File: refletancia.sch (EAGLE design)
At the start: 27 parts

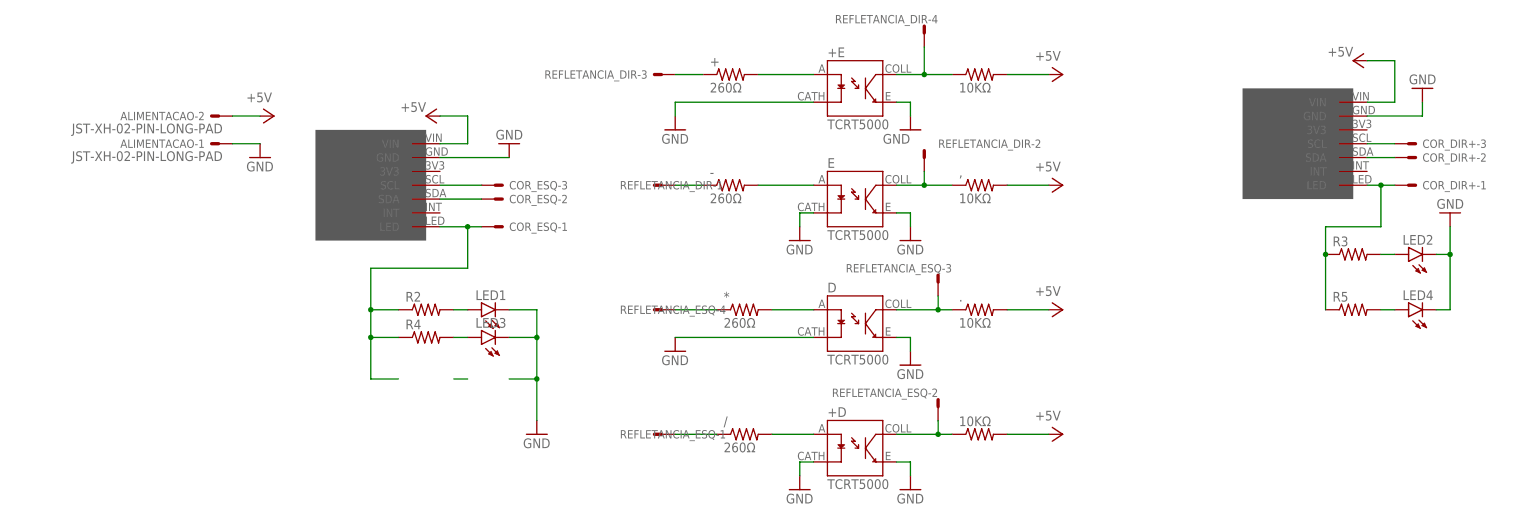
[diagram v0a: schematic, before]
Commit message: Alteração da dimensão e posição de furos
Os furos de fixação foram alterados, a posição dos conectores do sensor de cor também foi alterada, a dimensão da placa também foi alterada assim como posição de várias trilhas foi trocada
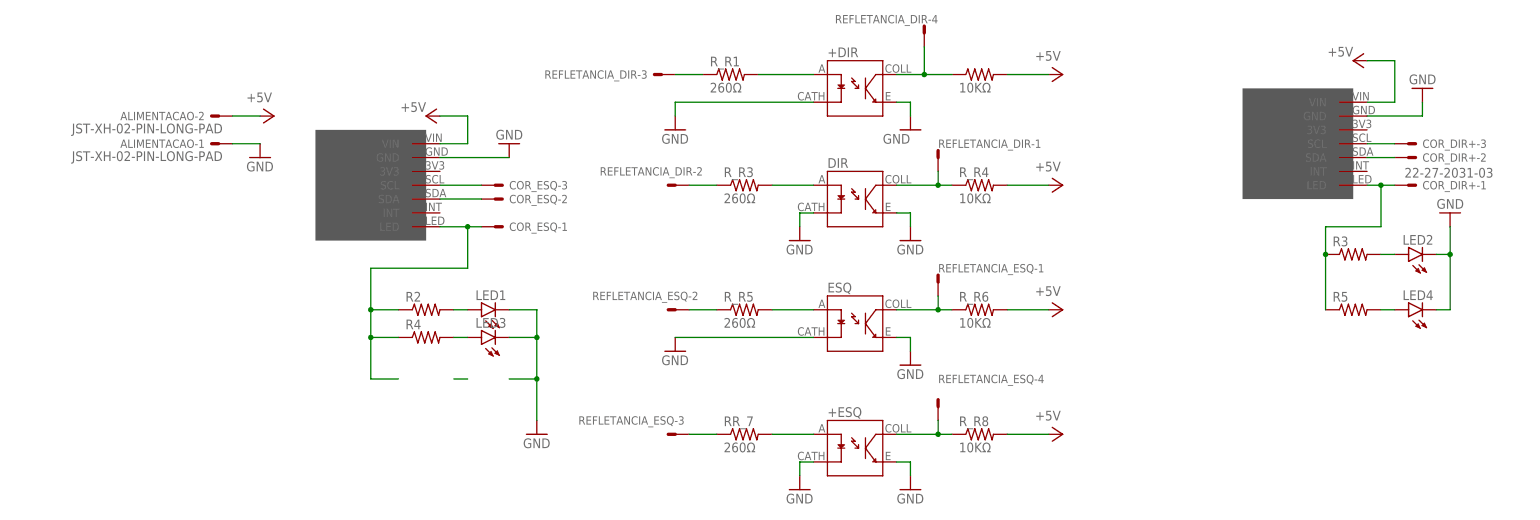
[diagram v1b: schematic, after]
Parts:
- removed -: 260Ω, rcl_robotica:R-US_0204/7
- removed .: 10KΩ, rcl_robotica:R-US_0204/7
- added R_R3: 260Ω, rcl_vitoria:R-US_0414/15_LONG_PAD
- added R_R6: 10KΩ, rcl_vitoria:R-US_0207/7_LONG_PAD2
- R_R8: value (none) -> 10KΩ
- renumbered * to R_R5, + to R_R1, +D to +ESQ, +E to +DIR, , to R_R4, / to RR_7, 10KΩ to R_R8, D to ESQ, E to DIR, R1 to R_R2
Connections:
- net +5V: now also R_R6.2; no longer ..2
- net ANALOG_+ESQ: now also REFLETANCIA_ESQ-4.S; no longer REFLETANCIA_ESQ-2.S
- net ANALOG_DIR: now also REFLETANCIA_DIR-1.S; no longer REFLETANCIA_DIR-2.S
- net ANALOG_ESQ: now also REFLETANCIA_ESQ-1.S, R_R6.1; no longer ..1, REFLETANCIA_ESQ-3.S
- net DIGITAL_+ESQ: now also REFLETANCIA_ESQ-3.S; no longer REFLETANCIA_ESQ-1.S
- net DIGITAL_DIR: now also REFLETANCIA_DIR-2.S, R_R3.1; no longer -.1, REFLETANCIA_DIR-1.S
- net DIGITAL_ESQ: now also REFLETANCIA_ESQ-2.S; no longer REFLETANCIA_ESQ-4.S
- net N$2: now also R_R3.2; no longer -.2
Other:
- moved on the sheet: REFLETANCIA_DIR-1, REFLETANCIA_DIR-2, REFLETANCIA_ESQ-1, REFLETANCIA_ESQ-2, REFLETANCIA_ESQ-3, REFLETANCIA_ESQ-4
